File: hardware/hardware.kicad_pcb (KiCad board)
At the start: 2 copper layers, 32 x 42 mm, 72 parts, among them J1 VCC, J10 Conn_01x05_Pin, J2 GND, J3 PHASE_A, J4 PHASE_B, J5 PHASE_C, J6 VBAT+, J7 GND, Q1 SiR158DP, Q10 SiR158DP, Q2 SiR158DP, Q3 SiR158DP, Q4 SiR158DP, Q5 SiR158DP, Q7 BC817, Q8 BC817, Q9 BC817, U1 ATmega8A-A, U2 ACS7122, U3 TPS709, Y1 16Mhz

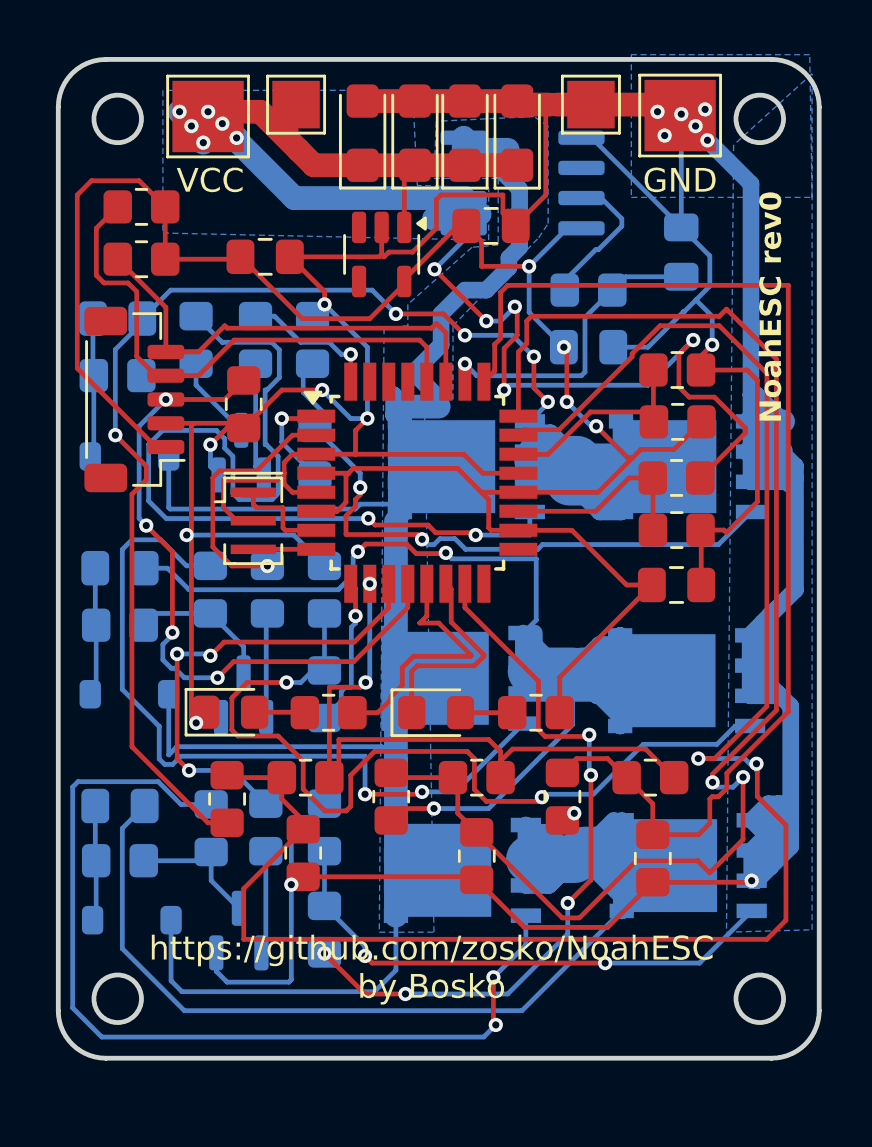
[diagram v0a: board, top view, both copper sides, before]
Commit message: add rev1 board - single side
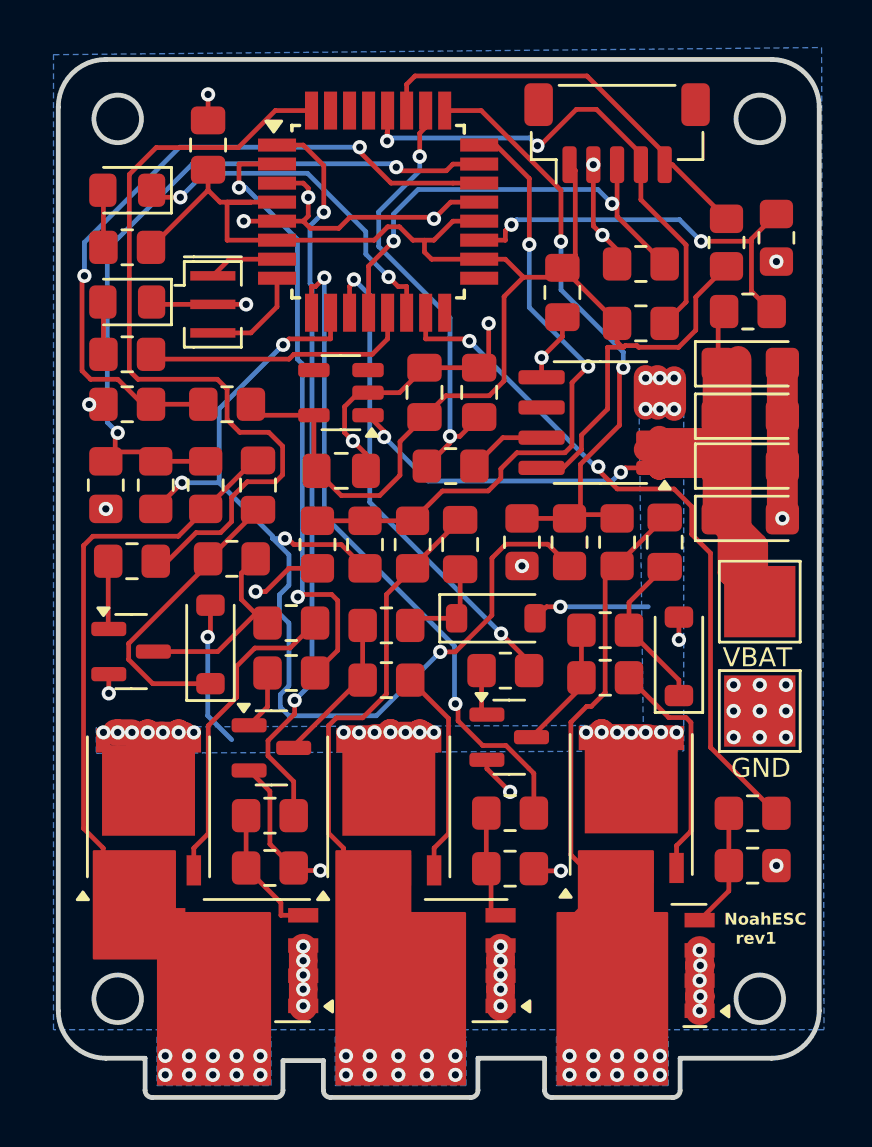
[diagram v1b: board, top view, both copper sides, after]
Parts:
- removed J3: PHASE_A, TestPoint:TestPoint_Pad_1.0x1.0mm
- removed J4: PHASE_B, TestPoint:TestPoint_Pad_1.0x1.0mm
- removed J5: PHASE_C, TestPoint:TestPoint_Pad_1.0x1.0mm
- removed J6: VBAT+, TestPoint:TestPoint_Pad_2.0x2.0mm
- removed J7: GND, TestPoint:TestPoint_Pad_2.0x2.0mm
- C11, C12, C13, C4, C5, D3, D4, D5, Q1, Q10, Q2, Q3, Q4, Q5, Q7, Q8, Q9, R20, R21, R22, R23, R24, R25, R26, R27, R28, R29, R30, R31, R32, R33, R34, R7, U2: moved to F.Cu
- J1: value VCC -> VBAT
- moved J1 30.9 mm to (126.2, 83.1)
- moved Q1 28.0 mm to (104.3, 98.2)
- moved R5 26.0 mm to (99.6, 68.2)
- moved D5 25.5 mm to (122.8, 85.4), turned to 90 degrees
- moved D1 25.5 mm to (99.6, 65.8), turned to 180 degrees
- moved C13 25.5 mm to (122.2, 80.6), turned to -90 degrees
- moved J2 25.3 mm to (126.2, 87.7)
- moved R2 24.6 mm to (124.8, 68.0), turned to -90 degrees
- moved J10 23.2 mm to (120.2, 63.4), turned to 0 degrees
- moved TH1 23.2 mm to (99.6, 74.8), turned to 180 degrees
- moved R33 22.6 mm to (119.7, 84.3), turned to 180 degrees
- moved R21 22.3 mm to (105.6, 94.3), turned to 0 degrees
- moved R3 21.6 mm to (121.2, 71.4), turned to 180 degrees
- moved Q10 19.6 mm to (100.5, 91.7), turned to 90 degrees
- moved C9 19.0 mm to (125.8, 73.1), turned to 0 degrees
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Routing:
- net GND: track 237.3 -> 66.3 mm, vias 15 -> 45
- net VBAT: track 82.1 -> 37.9 mm, vias 0 -> 30
- net SENSE_A: track 74.5 -> 30.6 mm
- net PHASE_C: track 56.7 -> 22.2 mm, vias 1 -> 10
- net GATE_BL: track 36.8 -> 4.78 mm, vias 2 -> 0
- net SENSE_B: track 58.7 -> 27.5 mm
- net GATE_CH: track 39.3 -> 9.75 mm, vias 2 -> 0
- net PHASE_A: track 65.7 -> 36.4 mm, vias 5 -> 10
- net PWM_AH: track 5.82 -> 34.2 mm, vias 1 -> 0
- net PWM_AL: track 4.46 -> 31.1 mm, vias 1 -> 2
- net PHASE_B: track 57.0 -> 31.5 mm, vias 3 -> 10
- net GATE_AH: track 38.7 -> 13.4 mm, vias 2 -> 0
- net SENSE_C: track 49.1 -> 25.9 mm, vias 0 -> 2
- net GATE_BH: track 32.2 -> 8.92 mm, vias 2 -> 0
- net PWM_BL: track 6.40 -> 28.6 mm, vias 1 -> 2
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- added copper zone on B.Cu, net PHASE_A
- added copper zone on B.Cu, net PHASE_B
- added copper zone on B.Cu, net PHASE_C
- removed copper zone on B.Cu, net VBAT+
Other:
- board size 32 x 42 mm -> 32 x 43.7 mm
- board text added: "NoahESC rev1"
- board text removed: "NoahESC rev0"

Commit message: add rev2
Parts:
- removed C4: 0.1uF, Capacitor_SMD:C_0805_2012Metric_Pad1.18x1.45mm_HandSolder
- removed C5: 1uF, Capacitor_SMD:C_0805_2012Metric_Pad1.18x1.45mm_HandSolder
- removed C6, C7, C8, C9: 100uF, Capacitor_Tantalum_SMD:CP_EIA-3216-10_Kemet-I
- removed D1: BLUE, LED_SMD:LED_0805_2012Metric_Pad1.15x1.40mm_HandSolder
- removed D2: RED, LED_SMD:LED_0805_2012Metric_Pad1.15x1.40mm_HandSolder
- removed J10: Conn_01x05_Pin, Connector_JST:JST_SH_BM05B-SRSS-TB_1x05-1MP_P1.00mm_Vertical
- removed R10, R8: 3.3K, Resistor_SMD:R_0805_2012Metric_Pad1.20x1.40mm_HandSolder
- removed R2, R3, TH1: 10K, Resistor_SMD:R_0805_2012Metric_Pad1.20x1.40mm_HandSolder
- removed R5: 1K, Resistor_SMD:R_0805_2012Metric_Pad1.20x1.40mm_HandSolder
- removed R6: 4.7K, Resistor_SMD:R_0805_2012Metric_Pad1.20x1.40mm_HandSolder
- removed R7: 47K, Resistor_SMD:R_0805_2012Metric_Pad1.20x1.40mm_HandSolder
- removed R9: 18K, Resistor_SMD:R_0805_2012Metric_Pad1.20x1.40mm_HandSolder
- removed U2: ACS7122, Package_SO:SOIC-8_3.9x4.9mm_P1.27mm
- added GND: GND, TestPoint:TestPoint_Keystone_5015_Micro-Minature, F.Cu at (102.1, 63.0)
- added PWM: PWM, TestPoint:TestPoint_Keystone_5015_Micro-Minature, F.Cu at (104.9, 63.0)
- moved J2 26.2 mm to (117.9, 62.8)
- moved J1 20.7 mm to (122.2, 62.8)
- moved C2 18.8 mm to (119.4, 73.0)
- moved U3 18.6 mm to (126.0, 67.6), turned to -90 degrees
- moved C10 18.5 mm to (126.0, 71.1), turned to 0 degrees
- moved R4 17.8 mm to (103.5, 66.6)
- moved R30 10.3 mm to (125.8, 85.3)
- moved Q9 10.2 mm to (125.9, 88.6), turned to 90 degrees
- moved Q8 10.2 mm to (115.8, 88.5), turned to 90 degrees
- moved R25 9.25 mm to (115.7, 85.1)
- moved R22 6.96 mm to (105.7, 85.1)
- moved Q7 6.77 mm to (105.6, 88.6), turned to 90 degrees
- moved R23 6.39 mm to (100.4, 85.9)
- moved C13 4.38 mm to (126.1, 78.6)
- moved R13 4.38 mm to (122.1, 78.6)
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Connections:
- J1 pad 1: VBAT+ -> VBAT
- U1 pad 13: LED_WARN -> unconnected-(U1-PB1-Pad13)
- U1 pad 14: LED_STATUS -> unconnected-(U1-PB2-Pad14)
- U1 pad 19: VBAT_ADC -> unconnected-(U1-ADC6-Pad19)
- U1 pad 22: TEMP_ADC -> unconnected-(U1-ADC7-Pad22)
- U1 pad 26: CURRENT_ADC -> unconnected-(U1-PC3-Pad26)
- U1 pad 27: SDA -> unconnected-(U1-PC4-Pad27)
- U1 pad 28: SCL -> unconnected-(U1-PC5-Pad28)
- U3 pad 1: VBAT+ -> VBAT
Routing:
- net VBAT+: track 46.8 -> 0.00 mm, vias 2 -> 0
- net 5V: track 72.4 -> 32.8 mm
- net GND: track 66.3 -> 32.2 mm, vias 45 -> 35
- net TEMP_ADC: track 30.1 -> 0.00 mm, vias 2 -> 0
- net SCL: track 21.8 -> 0.00 mm, vias 2 -> 0
- net CURRENT_ADC: track 19.0 -> 0.00 mm, vias 2 -> 0
- net SDA: track 17.5 -> 0.00 mm
- net VBAT_ADC: track 17.3 -> 0.00 mm, vias 2 -> 0
- net CENTER: track 45.9 -> 30.5 mm, vias 4 -> 3
- net LED_STATUS: track 14.9 -> 0.00 mm, vias 2 -> 0
- net PHASE_C: track 22.2 -> 34.2 mm
- net LED_WARN: track 11.5 -> 0.00 mm
- net VBAT: track 37.9 -> 27.7 mm, vias 30 -> 23
- net PWM_AH: track 34.2 -> 27.3 mm
- net PWM_BL: track 28.6 -> 21.8 mm, vias 2 -> 0
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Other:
- board text added: "NoahESC rev2"
- board text removed: "NoahESC rev1"
